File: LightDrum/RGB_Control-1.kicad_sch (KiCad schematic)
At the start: 25 parts, among them U301 PCA9634_TSSOP20, U302 SQ2310ES_SOT23, U303 SQ2310ES_SOT23, U304 SQ2310ES_SOT23, U305 SQ2310ES_SOT23, U306 SQ2310ES_SOT23, U307 SQ2310ES_SOT23, U308 SQ2310ES_SOT23, U309 SQ2310ES_SOT23

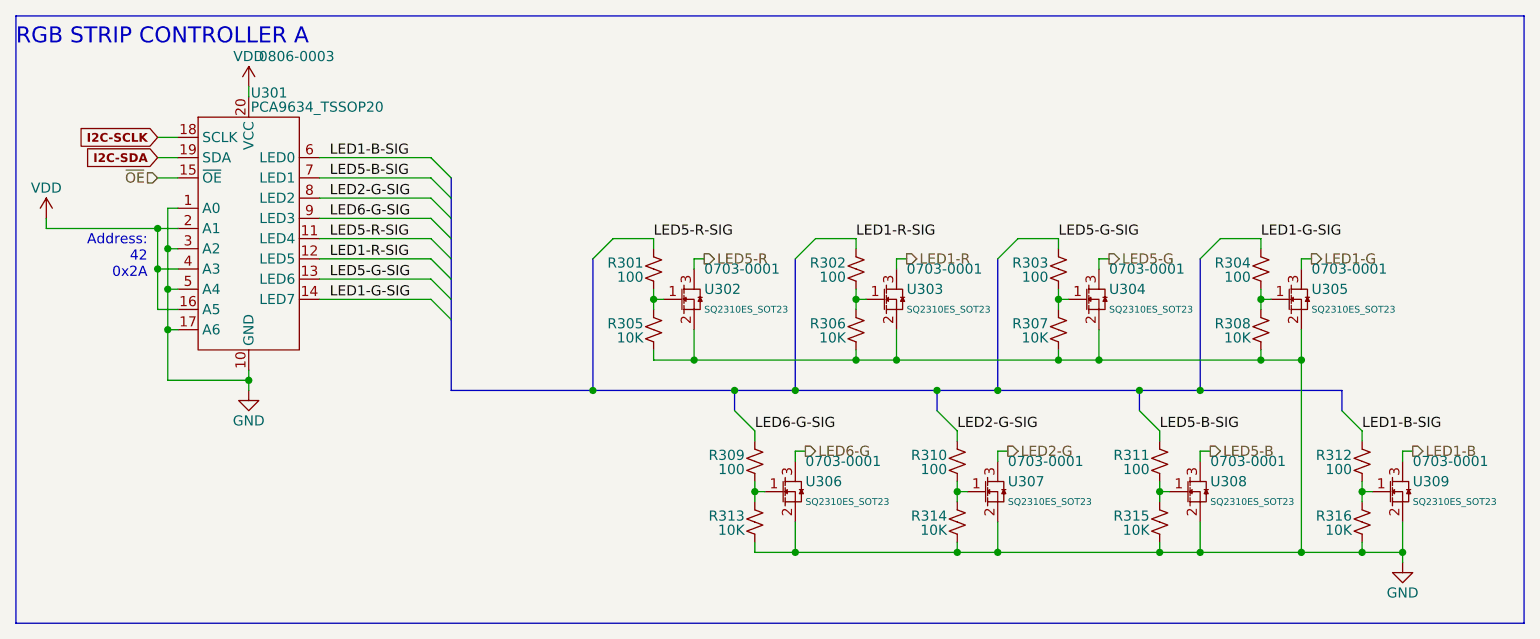
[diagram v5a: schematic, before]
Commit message: Replace old MOSFETs with a more compact package
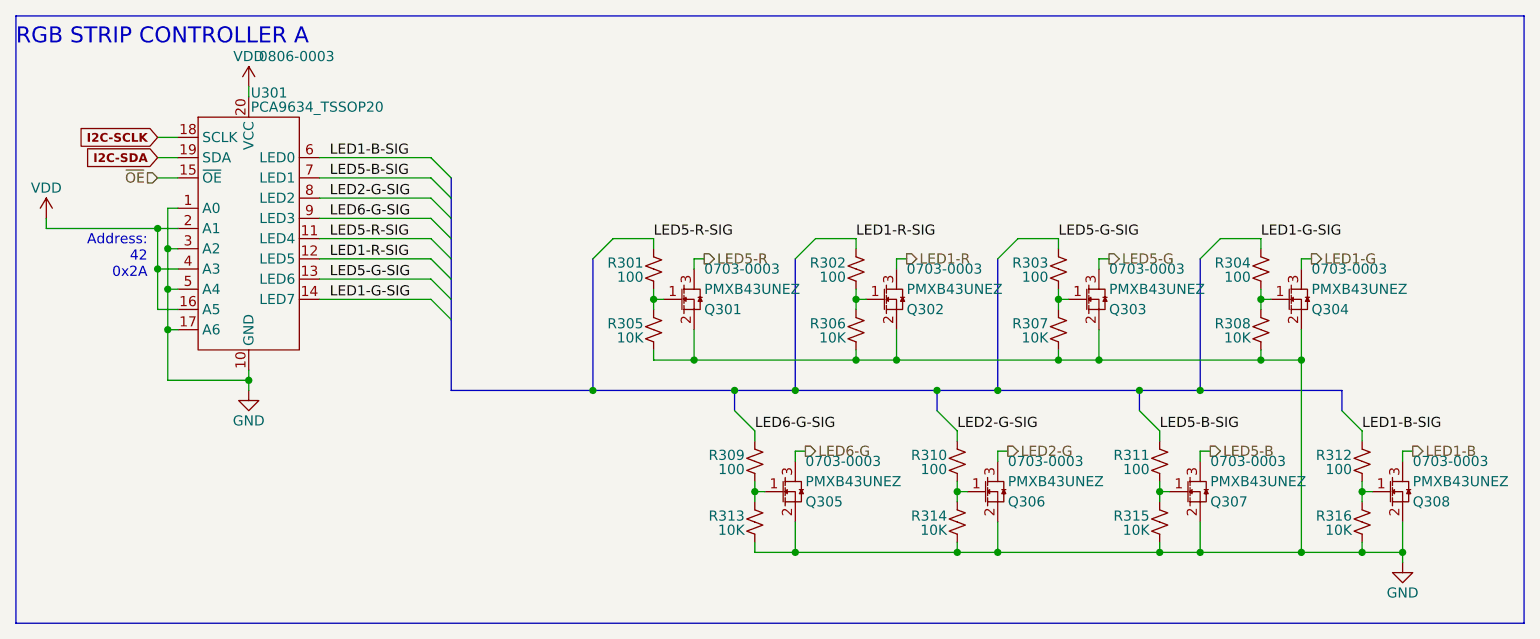
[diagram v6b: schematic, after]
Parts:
- removed U302, U303, U304, U305, U306, U307, U308, U309: SQ2310ES_SOT23, Package_TO_SOT_SMD:SOT-23, symbol Daxxn_Transistors:SQ2310ES_SOT23
- added Q301, Q302, Q303, Q304, Q305, Q306, Q307, Q308: PMXB43UNEZ, Daxxn_Packages:DFN1010D-3, symbol Daxxn_Transistors:PMXB43UNEZ
- R301, R302, R303, R304, R305, R306, R307, R308, R309, R310, R311, R312, R313, R314, R315, R316: footprint Resistor_SMD:R_0805_2012Metric -> Resistor_SMD:R_0603_1608Metric
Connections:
- net GND: now also Q301.2 (S), Q302.2 (S), Q303.2 (S), Q304.2 (S), Q305.2 (S), Q306.2 (S), Q307.2 (S), Q308.2 (S)
- net LED1-B: now also Q308.3 (D)
- net LED1-G: now also Q304.3 (D)
- net LED1-R: now also Q302.3 (D)
- net LED2-G: now also Q306.3 (D)
- net LED5-B: now also Q307.3 (D)
- net LED5-G: now also Q303.3 (D)
- net LED5-R: now also Q301.3 (D)
- net LED6-G: now also Q305.3 (D)
- net at R309.2, R313.1: now also Q305.1 (G)
- net at R312.2, R316.1: now also Q308.1 (G)
- net at R304.2, R308.1: now also Q304.1 (G)
- net at R302.2, R306.1: now also Q302.1 (G)
- net at R310.2, R314.1: now also Q306.1 (G)
- net at R303.2, R307.1: now also Q303.1 (G)
- net at R311.2, R315.1: now also Q307.1 (G)
- net at R301.2, R305.1: now also Q301.1 (G)

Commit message: Lock REV8 Layout and send to PCB MNF
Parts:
- R301, R302, R303, R304, R305, R306, R307, R308, R309, R310, R311, R312, R313, R314, R315, R316: footprint Resistor_SMD:R_0603_1608Metric -> Resistor_SMD:R_0402_1005Metric
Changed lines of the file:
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@@
       (effects (font (size 1.27 1.27)) (justify right))
     )
-    (property "Footprint" "Resistor_SMD:R_0603_1608Metric" (id 2) (at 109.22 72.39 0)
+    (property "Footprint" "Resistor_SMD:R_0402_1005Metric" (id 2) (at 109.22 72.39 0)
       (effects (font (size 1.27 1.27)) hide)
     )
@@
       (effects (font (size 1.27 1.27)) (justify right))
     )
-    (property "Footprint" "Resistor_SMD:R_0603_1608Metric" (id 2) (at 185.42 72.39 0)
+    (property "Footprint" "Resistor_SMD:R_0402_1005Metric" (id 2) (at 185.42 72.39 0)
       (effects (font (size 1.27 1.27)) hide)
     )
@@
       (effects (font (size 1.27 1.27)) (justify right))
     )
-    (property "Footprint" "Resistor_SMD:R_0603_1608Metric" (id 2) (at 172.72 55.88 0)
+    (property "Footprint" "Resistor_SMD:R_0402_1005Metric" (id 2) (at 172.72 55.88 0)
       (effects (font (size 1.27 1.27)) hide)
     )
@@
       (effects (font (size 1.27 1.27)) (justify right))
     )
-    (property "Footprint" "Resistor_SMD:R_0603_1608Metric" (id 2) (at 109.22 80.01 0)
+    (property "Footprint" "Resistor_SMD:R_0402_1005Metric" (id 2) (at 109.22 80.01 0)
       (effects (font (size 1.27 1.27)) hide)
     )
@@
       (effects (font (size 1.27 1.27)) (justify right))
     )
-    (property "Footprint" "Resistor_SMD:R_0603_1608Metric" (id 2) (at 172.72 48.26 0)
+    (property "Footprint" "Resistor_SMD:R_0402_1005Metric" (id 2) (at 172.72 48.26 0)
       (effects (font (size 1.27 1.27)) hide)
     )
@@
       (effects (font (size 1.27 1.27)) (justify right))
     )
-    (property "Footprint" "Resistor_SMD:R_0603_1608Metric" (id 2) (at 121.92 55.88 0)
+    (property "Footprint" "Resistor_SMD:R_0402_1005Metric" (id 2) (at 121.92 55.88 0)
       (effects (font (size 1.27 1.27)) hide)
     )
@@
       (effects (font (size 1.27 1.27)) (justify right))
     )
-    (property "Footprint" "Resistor_SMD:R_0603_1608Metric" (id 2) (at 134.62 80.01 0)
+    (property "Footprint" "Resistor_SMD:R_0402_1005Metric" (id 2) (at 134.62 80.01 0)
       (effects (font (size 1.27 1.27)) hide)
     )
@@
       (effects (font (size 1.27 1.27)) (justify right))
     )
-    (property "Footprint" "Resistor_SMD:R_0603_1608Metric" (id 2) (at 160.02 80.01 0)
+    (property "Footprint" "Resistor_SMD:R_0402_1005Metric" (id 2) (at 160.02 80.01 0)
       (effects (font (size 1.27 1.27)) hide)
     )
@@
       (effects (font (size 1.27 1.27)) (justify right))
     )
-    (property "Footprint" "Resistor_SMD:R_0603_1608Metric" (id 2) (at 160.02 72.39 0)
+    (property "Footprint" "Resistor_SMD:R_0402_1005Metric" (id 2) (at 160.02 72.39 0)
       (effects (font (size 1.27 1.27)) hide)
     )
@@
       (effects (font (size 1.27 1.27)) (justify right))
     )
-    (property "Footprint" "Resistor_SMD:R_0603_1608Metric" (id 2) (at 121.92 48.26 0)
+    (property "Footprint" "Resistor_SMD:R_0402_1005Metric" (id 2) (at 121.92 48.26 0)
       (effects (font (size 1.27 1.27)) hide)
     )
@@
       (effects (font (size 1.27 1.27)) (justify right))
     )
-    (property "Footprint" "Resistor_SMD:R_0603_1608Metric" (id 2) (at 96.52 48.26 0)
+    (property "Footprint" "Resistor_SMD:R_0402_1005Metric" (id 2) (at 96.52 48.26 0)
       (effects (font (size 1.27 1.27)) hide)
     )
@@
       (effects (font (size 1.27 1.27)) (justify right))
     )
-    (property "Footprint" "Resistor_SMD:R_0603_1608Metric" (id 2) (at 96.52 55.88 0)
+    (property "Footprint" "Resistor_SMD:R_0402_1005Metric" (id 2) (at 96.52 55.88 0)
       (effects (font (size 1.27 1.27)) hide)
     )
@@
       (effects (font (size 1.27 1.27)) (justify right))
     )
-    (property "Footprint" "Resistor_SMD:R_0603_1608Metric" (id 2) (at 185.42 80.01 0)
+    (property "Footprint" "Resistor_SMD:R_0402_1005Metric" (id 2) (at 185.42 80.01 0)
       (effects (font (size 1.27 1.27)) hide)
     )
@@
       (effects (font (size 1.27 1.27)) (justify right))
     )
-    (property "Footprint" "Resistor_SMD:R_0603_1608Metric" (id 2) (at 147.32 55.88 0)
+    (property "Footprint" "Resistor_SMD:R_0402_1005Metric" (id 2) (at 147.32 55.88 0)
       (effects (font (size 1.27 1.27)) hide)
     )
@@
       (effects (font (size 1.27 1.27)) (justify right))
     )
-    (property "Footprint" "Resistor_SMD:R_0603_1608Metric" (id 2) (at 134.62 72.39 0)
+    (property "Footprint" "Resistor_SMD:R_0402_1005Metric" (id 2) (at 134.62 72.39 0)
       (effects (font (size 1.27 1.27)) hide)
     )
@@
       (effects (font (size 1.27 1.27)) (justify right))
     )
-    (property "Footprint" "Resistor_SMD:R_0603_1608Metric" (id 2) (at 147.32 48.26 0)
-      (effects (font (size 1.27 1.27)) hide)
-    )
+    (property "Footprint" "Resistor_SMD:R_0402_1005Metric" (id 2) (at 147.32 48.26 0)
+      (effects (font (size 1.27 1.27)) hide)
+    )
